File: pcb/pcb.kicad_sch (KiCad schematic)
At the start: 2 parts, among them U1 ATtiny85-20P

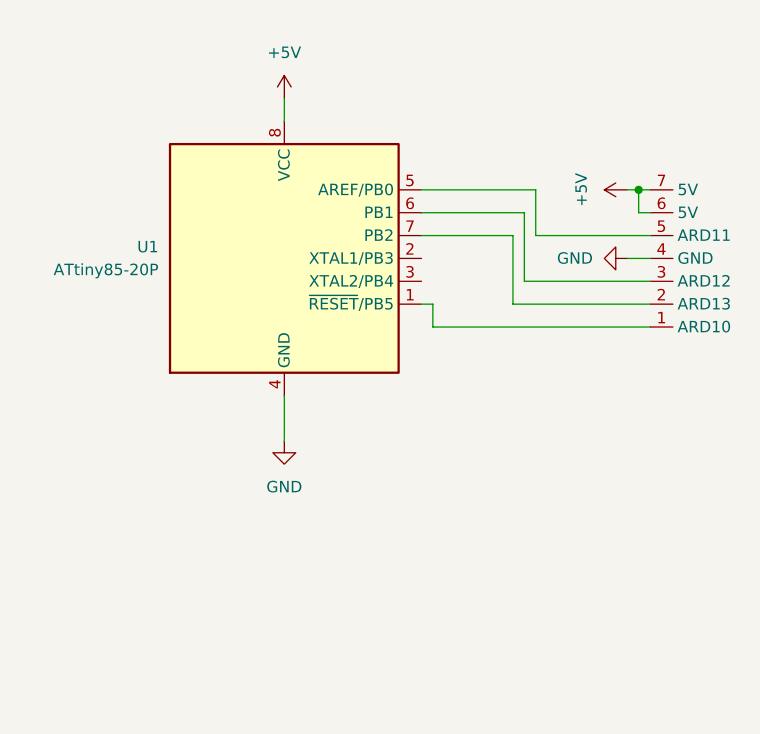
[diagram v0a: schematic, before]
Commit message: Add schematic
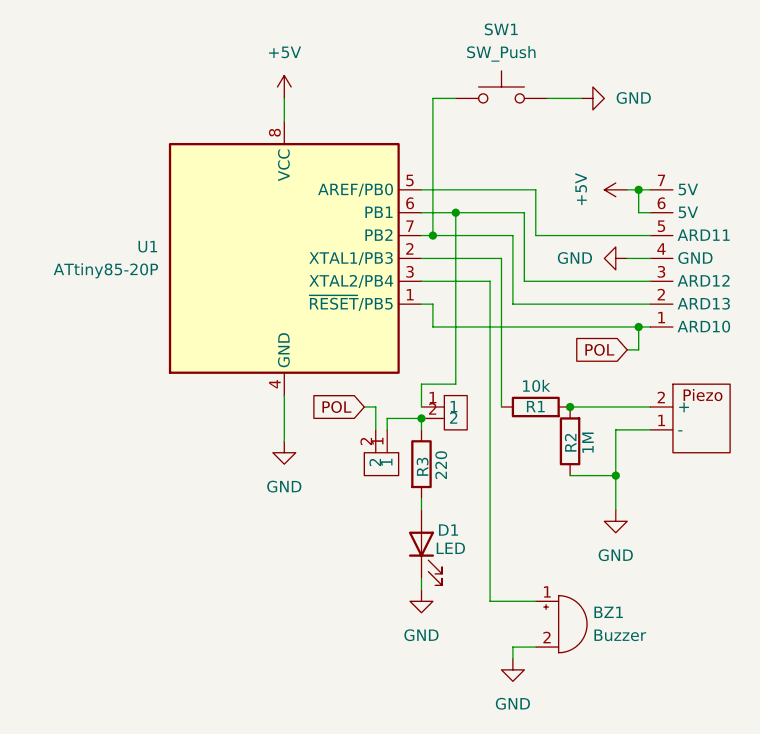
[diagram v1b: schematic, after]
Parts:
- added BZ1: Buzzer, symbol Device:Buzzer
- added D1: LED, LED_THT:LED_D5.0mm, symbol Device:LED
- added R1: 10k, Resistor_THT:R_Axial_DIN0207_L6.3mm_D2.5mm_P10.16mm_Horizontal, symbol Device:R
- added R2: 1M, Resistor_THT:R_Axial_DIN0207_L6.3mm_D2.5mm_P10.16mm_Horizontal, symbol Device:R
- added R3: 220, Resistor_THT:R_Axial_DIN0207_L6.3mm_D2.5mm_P10.16mm_Horizontal, symbol Device:R
- added SW1: SW_Push, symbol Switch:SW_Push
- added U3: ~, symbol Symbols:Piezo
- added U4, U5: ~, Library:Jumper, symbol Symbols:Jumper
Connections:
- net GND: now also BZ1.2 (-), D1.1 (K), R2.1, SW1.2, U3.1 (-)
- net POL: now reaches U1.1 (~{RESET}/PB5), U2.1 (ARD10)
- net POL: now also U5.2
- net at U1.7 (PB2), U2.2 (ARD13): now also SW1.1
- net at U1.6 (PB1), U2.3 (ARD12): now also U4.1
- net at U1.2 (XTAL1/PB3): now also R1.1
- net at U1.3 (XTAL2/PB4): now also BZ1.1 (+)
- new net: R3.1, U4.2, U5.1
- new net: D1.2 (A), R3.2
- new net: R1.2, R2.2, U3.2 (+)

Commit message: Add PCB draft
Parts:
- removed U4, U5: ~, Library:Jumper, symbol Symbols:Jumper
- BZ1: footprint (none) -> Buzzer_Beeper:Buzzer_15x7.5RM7.6
- SW1: footprint (none) -> Button_Switch_THT:SW_PUSH_6mm
- U3: footprint (none) -> Library:Piezo
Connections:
- net at U1.6 (PB1), U2.3 (ARD12): now also R3.1
- net POL: no longer names the net of U1.1 (~{RESET}/PB5), U2.1 (ARD10)

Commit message: Finish PCB design
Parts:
- R2: value 1M -> 10k
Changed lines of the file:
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@@
 			)
 		)
-		(property "Value" "1M"
+		(property "Value" "10k"
 			(at 164.5938 105.6064 90)
 			(effects
